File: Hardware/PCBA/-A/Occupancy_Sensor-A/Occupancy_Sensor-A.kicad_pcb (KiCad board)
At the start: 4 copper layers, 30 x 30 mm, 84 parts, among them J1 USB_C_Receptacle, J2 Conn_02x05_Odd_Even, J3 Conn_Coaxial, Q1 2N7002, Q2 2N7002, Q3 2N7002, Q4 2N7002, Q5 2N7002, Q6 DMG1012T, SW1 SW_Push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

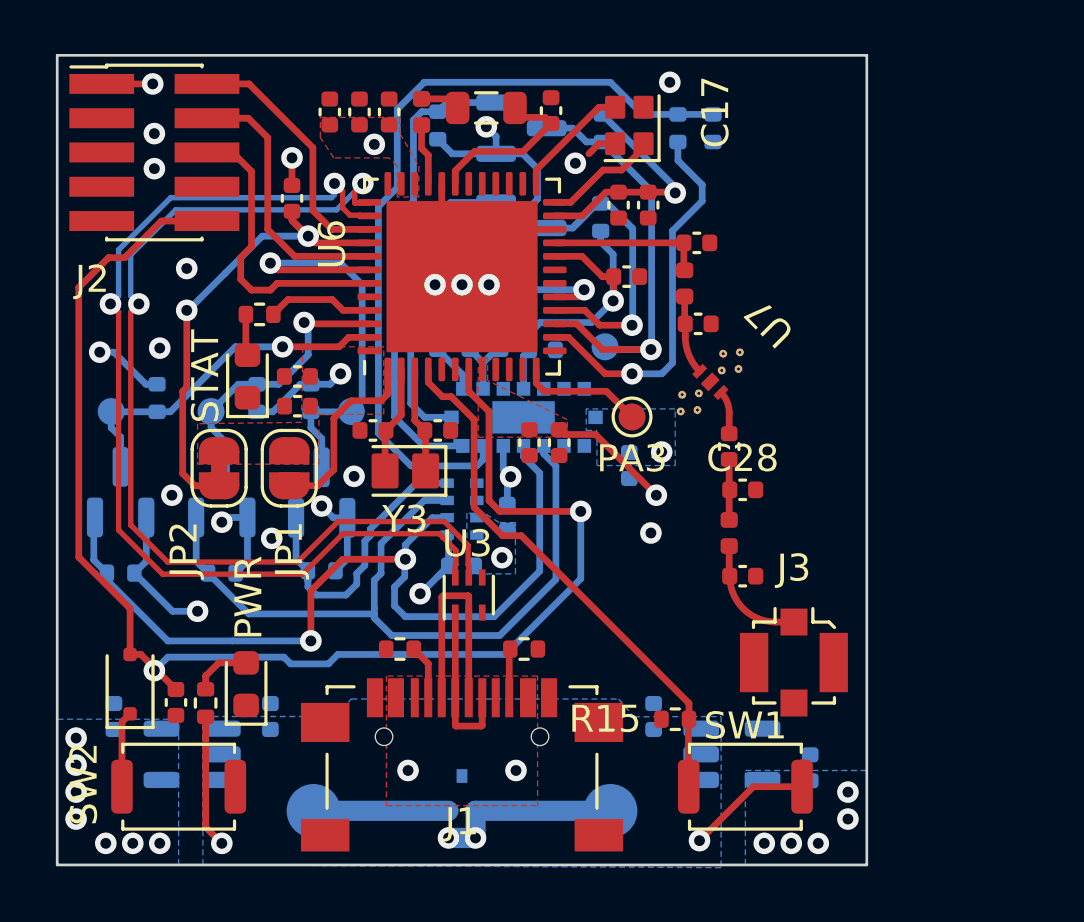
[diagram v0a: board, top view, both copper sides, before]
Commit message: IPEX socket PCB trace change
Changed the through hole path of the LFB182G45CGFD436 and reroute the PCB trace of the IPEX socket.
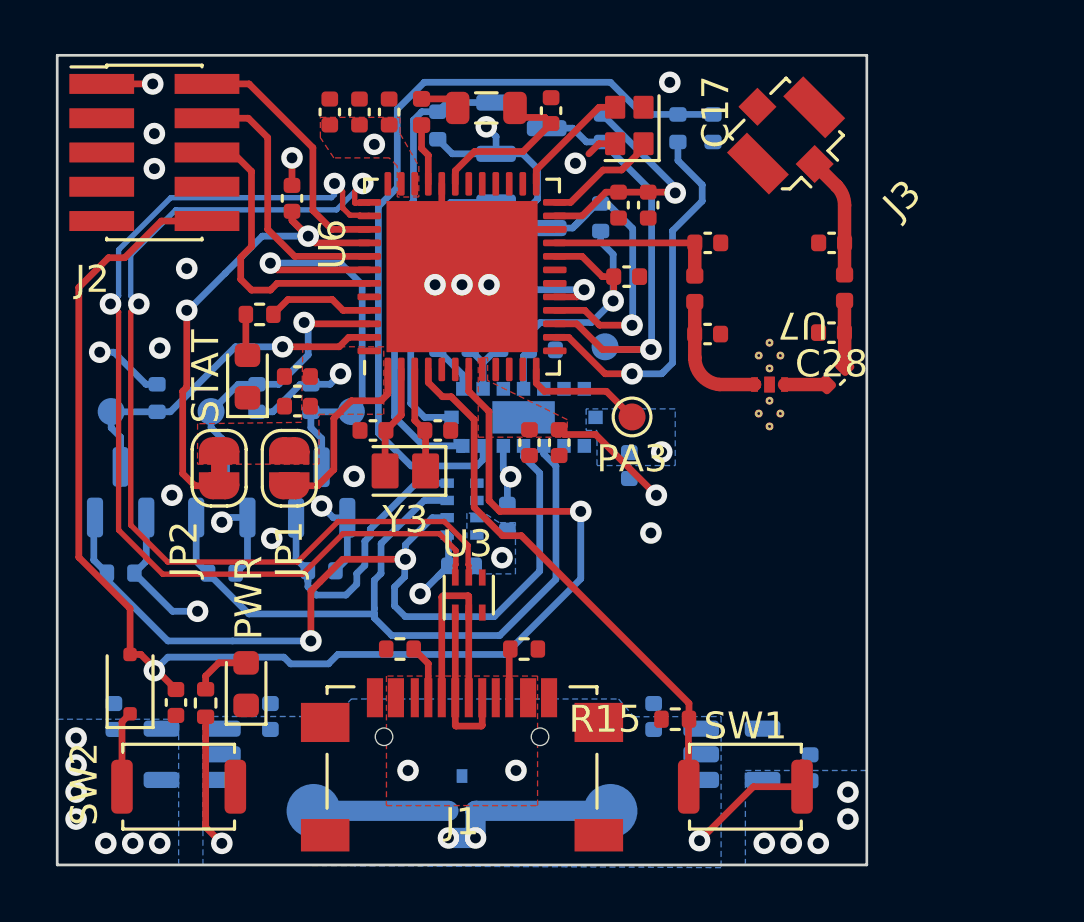
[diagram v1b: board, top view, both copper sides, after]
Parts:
- moved J3 19.5 mm to (157.0, 103.0), turned to 45 degrees
- moved C27 12.8 mm to (158.7, 107.0), turned to 180 degrees
- moved L4 10.0 mm to (159.2, 108.6), turned to 90 degrees
- moved C28 6.69 mm to (158.7, 110.3), turned to 180 degrees
- moved C26 4.74 mm to (158.8, 111.9), turned to 45 degrees
- moved U7 2.20 mm to (156.4, 112.2), turned to 180 degrees
- moved C25 0.52 mm to (154.1, 110.3)
- moved L3 0.43 mm to (153.6, 108.7)
- moved C24 0.41 mm to (154.1, 107.0)
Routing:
- net Net-(C25-Pad1): track 2.91 -> 4.82 mm
- net RF: track 5.60 -> 6.43 mm

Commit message: Final TOF sensor layout
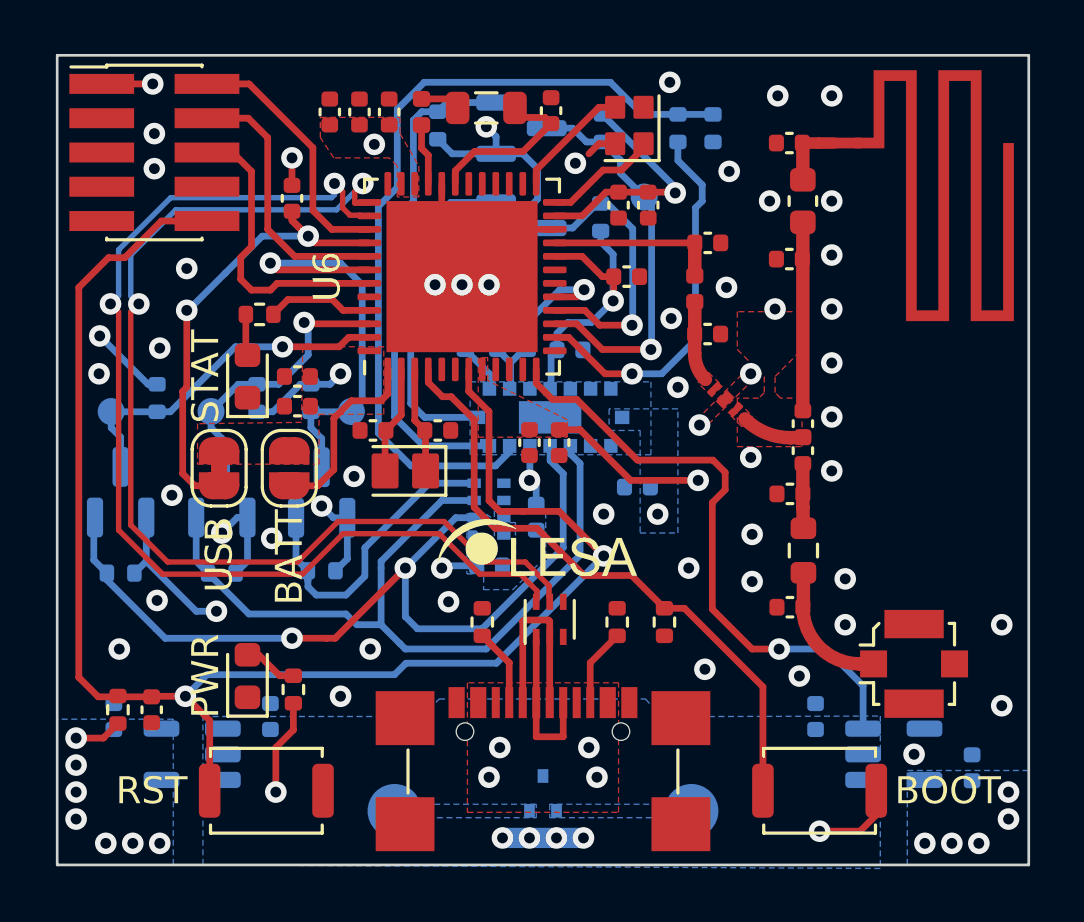
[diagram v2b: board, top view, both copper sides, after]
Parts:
- removed D3: BAT54J, Diode_SMD:D_SOD-323F
- removed TP6: PA3, TestPoint:TestPoint_Pad_D1.0mm
- added AE1: Antenna, Occupancy_Sensor_Custom_Footprints:AN3359_Meander_Antenna, F.Cu at (159.2, 103.2)
- added C29: ~, Capacitor_SMD:C_0402_1005Metric, F.Cu at (157.1, 107.5)
- added C30: 1.2pf, Capacitor_SMD:C_0402_1005Metric, F.Cu at (157.1, 103.2)
- added C31: 10nf, Capacitor_SMD:C_0402_1005Metric, F.Cu at (157.6, 114.7)
- added G***: LOGO, Occupancy_Sensor_Custom_Footprints:LESA_8x4mm, F.Cu at (147.9, 118.3)
- added L5: 3.6nH, Inductor_SMD:L_0603_1608Metric, F.Cu at (157.6, 105.4)
- added R21: 1K, Resistor_SMD:R_0402_1005Metric, F.Cu at (132.2, 124.2)
- C27: value 1.2pf -> ~
- J1: footprint Occupancy_Sensor_Custom_Footprints:TYPEC-304S-ACP16 -> Occupancy_Sensor_Custom_Footprints:USB4110-GF-A
- JP1: value Jumper_2_Open -> BATT
- JP2: value Jumper_2_Bridged -> USB
- L4: value 3.6nH -> 0R; footprint Inductor_SMD:L_0402_1005Metric -> Resistor_SMD:R_0603_1608Metric
- SW1: value SW_Push -> BOOT
- SW2: value SW_Push -> RST
- moved J3 20.1 mm to (161.8, 122.5), turned to -90 degrees
- moved C27 13.6 mm to (157.2, 120.5)
- moved L4 9.86 mm to (157.7, 118.3), turned to -90 degrees
- moved C28 6.17 mm to (157.2, 116.2)
- moved C6 6.00 mm to (158.1, 124.5)
- moved C7 6.00 mm to (163.9, 126.4)
- moved U4 6.00 mm to (161.0, 125.9)
- moved TP5 5.74 mm to (151.8, 105.2)
- moved J1 3.87 mm to (148.0, 131.3)
- moved R15 3.62 mm to (152.5, 121.0), turned to -90 degrees
- moved R2 3.59 mm to (150.8, 121.0), turned to 90 degrees
- moved R8 3.29 mm to (138.8, 123.5)
- moved SW2 3.25 mm to (137.8, 127.2)
- moved R1 3.21 mm to (145.8, 121.0), turned to 90 degrees
- moved U3 3.13 mm to (148.2, 120.9)
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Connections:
- C28 pad 1: Net-(C26-Pad2) -> Net-(C28-Pad1)
- L4 pad 1: Net-(C26-Pad2) -> Net-(C28-Pad1)
- SW2 pad 2: Net-(D3-K) -> NRST
- U4 pad 3: /1V8_EN -> 1V8_EN
- U6 pad 12: Net-(U6-PA3) -> 1V8_EN
- U6 pad 30: /PE4 -> unconnected-(U6-PE4-Pad30)
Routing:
- net 1V8_EN: track 0.00 -> 22.5 mm, vias 0 -> 1
- net +1V8: track 76.3 -> 95.8 mm
- net NRST: track 51.0 -> 56.3 mm
- net Net-(C26-Pad2): track 2.43 -> 7.27 mm
- net Net-(U6-PA3): track 4.58 -> 0.00 mm
- net Net-(Q6-S): track 4.50 -> 0.00 mm
- net Net-(AE1-A): track 0.00 -> 3.56 mm
- net BOOT: track 20.1 -> 23.3 mm
- net USB_P: track 37.1 -> 40.2 mm
- net USB_N: track 36.9 -> 39.9 mm
- net GND: track 17.1 -> 14.1 mm, vias 17 -> 51
- net Net-(D3-K): track 2.82 -> 0.00 mm
- net Net-(C28-Pad1): track 0.00 -> 2.40 mm
- net Net-(U3-D-_in): track 8.52 -> 6.47 mm
- net Net-(C25-Pad1): track 4.82 -> 2.98 mm
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- added copper zone on In2.Cu, net GND
- added copper zone on F.Cu, net Net-(C25-Pad1)
- added copper zone on F.Cu, net Net-(C26-Pad1)
- added copper zone on B.Cu, net Net-(Q6-S)
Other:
- board size 30 x 30 mm -> 36 x 30 mm

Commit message: Add Gerbers, PnP, BOM, PDFs for -A rev
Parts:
- removed J1: USB_C_Receptacle, Occupancy_Sensor_Custom_Footprints:USB4110-GF-A
- removed Q5: 2N7002, Package_TO_SOT_SMD:SOT-23
- removed U7: ~, Occupancy_Sensor_Custom_Footprints:LFB182G45CGFD436
- added J4: USB_C_Receptacle, Occupancy_Sensor_Custom_Footprints:USB4120-03-C, F.Cu at (148.0, 126.2)
- added Q7: BSS138, Package_TO_SOT_SMD:SOT-23, B.Cu at (132.3, 116.2)
- added U8: DEA162450BT-1295A1, Occupancy_Sensor_Custom_Footprints:DEA162450BT-1295A1, F.Cu at (154.7, 112.7)
- C24: value 0.8pf -> 0.8p
- C25: value 0.3pf -> 0.3p
- C26, C31: value 10nf -> 10n
- C30: value 1.2pf -> 1.2p
- J3: footprint Connector_Coaxial:U.FL_Molex_MCRF_73412-0110_Vertical -> Occupancy_Sensor_Custom_Footprints:CONUFL001-SMD-T
- L3: value 2.7nH -> 2.7n
- L5: value 3.6nH -> 3.6n; footprint Inductor_SMD:L_0603_1608Metric -> Inductor_SMD:L_0402_1005Metric
- Q1, Q2, Q3, Q4: value 2N7002 -> BSS138
- Q6, TP1, TP2: moved to F.Cu
- R11, R4: value 40K -> 40.2K
- SW1, SW2: footprint Button_Switch_SMD:SW_Push_SPST_NO_Alps_SKRK -> Occupancy_Sensor_Custom_Footprints:EVQ-P7A01P
- U4: value TPS7A03185PDQNR -> TPS7A0318PDBVR
- moved Q6 10.7 mm to (137.4, 125.6)
- moved R2 7.99 mm to (154.0, 128.3), turned to 0 degrees
- moved R1 2.65 mm to (143.8, 122.8), turned to 180 degrees
- moved TP1 2.22 mm to (141.2, 126.2)
- moved TP2 2.22 mm to (154.8, 126.2), turned to 0 degrees
- moved SW1 1.35 mm to (158.5, 128.6)
- moved SW2 1.27 mm to (137.5, 128.5), turned to 0 degrees
- moved D1 0.40 mm to (137.1, 122.6)
- moved R8 0.30 mm to (138.7, 123.2)
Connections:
- SW2 pad 1: GND -> NRST
- SW2 pad 2: NRST -> GND
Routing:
- net +1V8: track 95.8 -> 106.0 mm
- net Net-(U3-D+_in): track 6.11 -> 13.3 mm, vias 0 -> 2
- net Net-(U3-D-_in): track 6.47 -> 12.7 mm, vias 0 -> 2
- net BOOT: track 23.3 -> 27.7 mm
- net Net-(J4-CC2): track 2.64 -> 6.91 mm
- net NRST: track 56.3 -> 59.9 mm
- net VBUS: track 3.56 -> 0.00 mm, vias 5 -> 6
- net GND: track 14.1 -> 11.1 mm, vias 51 -> 50
- net Net-(J4-CC1): track 3.13 -> 4.83 mm
- net +3.3V: track 39.4 -> 40.0 mm
- net Net-(AE1-A): track 3.56 -> 4.11 mm
- added copper zone on F.Cu, net Net-(Q6-S)
- removed copper zone on B.Cu, net Net-(Q6-S)
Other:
- board text added: "1.0-A"
